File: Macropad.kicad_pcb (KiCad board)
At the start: 2 copper layers, 11 parts, among them SW1 SW_Push, SW2 SW_Push, SW3 SW_Push, SW4 SW_Push, SW5 SW_Push, U1 XIAO-RP2040-DIP

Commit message: added the libraries!!!
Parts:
- removed OL1: OLED, display:SSD1306_OLED-0.91-128x32
- added D5: SK6812MINI, LED_SMD:LED_SK6812MINI_PLCC4_3.5x3.5mm_P1.75mm, F.Cu at (191.8, 109.0)
- added J1: Conn_01x04, display:SSD1306-0.91-OLED-4pin-128x32, F.Cu at (165.8, 73.9)
- moved D1 101.6 mm to (115.5, 79.9)
- moved D3 59.5 mm to (114.5, 108.7)
- moved D2 58.4 mm to (92.1, 108.7), turned to 180 degrees
- moved SW2 56.9 mm to (111.1, 127.8), turned to 180 degrees
- moved SW1 56.3 mm to (90.0, 127.8), turned to 180 degrees
- moved SW5 48.5 mm to (94.8, 74.8)
- moved U1 37.7 mm to (142.7, 80.1)
- moved D4 25.8 mm to (171.4, 109.0)
- moved SW3 22.8 mm to (168.3, 127.8), turned to 180 degrees
- moved SW4 22.8 mm to (189.7, 127.8), turned to 180 degrees
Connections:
- D4 pad 1: unconnected-(D4-DOUT-Pad1) -> Net-(D4-DOUT)
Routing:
- net GND: track 0.00 -> 330.3 mm
- net +5V: track 0.00 -> 276.2 mm
- net Net-(U1-GPIO3/MOSI): track 0.00 -> 80.1 mm
- net Net-(J1-Pin_4): track 0.00 -> 76.1 mm
- net Net-(J1-Pin_3): track 0.00 -> 69.7 mm
- net Net-(U1-GPIO1/RX): track 0.00 -> 62.5 mm
- net Net-(U1-GPIO4/MISO): track 0.00 -> 62.3 mm
- net Net-(D3-DOUT): track 0.00 -> 62.2 mm
- net Net-(U1-GPIO0/TX): track 0.00 -> 51.0 mm
- net Net-(U1-GPIO2/SCK): track 0.00 -> 51.0 mm
- net Net-(D1-DOUT): track 0.00 -> 38.5 mm
- net Net-(D4-DOUT): track 0.00 -> 25.5 mm
- net Net-(D2-DOUT): track 0.00 -> 23.0 mm
- net Net-(D1-DIN): track 0.00 -> 19.1 mm
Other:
- board outline added: 132.6 x 63.9 mm
- board text added: "/ / , -‐─‐- ..__／'￣｀ ＿ , -‐ｧ′/／／ ￣￣｀ //⌒＝ミ, | | | ／ ./ / ／ ⌒＼＼| | | / .::| ｛// ／ ＼ｉ | | . / .: .:| 〃 ／ ／／ j | | | ′ .: .::｣_// ／ ,_／／〃 / i∨ハ i : .:| Y{ 〃__彡'＾く／/ //ii i ! |( ∨ / ! .::|||l.|｢ //ｨﾃそk 彡 / ／_⌒| ! j :| ｀. ∨ / . i |__/|: //|弋ｚｿ ／イｯ'てトJ / /} ハ : ∨ / . | :.:.V|/V｜ ヒ ｿ ﾉj/ /ｨ/ '. ∨ / . | :.:.:!i|l「ﾍ.ﾄ, ､ ' __ 〃 〃/{ :. : i∨ . | :.:.:.:|!ﾏ={{ ＼ ＿ｰ‐ |ｉｉ| .ｲ / /イ{｛ :. :. i'. / . | :.:.:.Vﾊ ＼/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"
- board text added: ":p"
- board text added: "CO0l macropad"
- board text added: "SHOUTOUT TO MY BESTIES TACO AND 1-15 :3"
- board text added: "XIAO HERE!"
- board text added: "thx to blueprint by hackclub and amd"
- board text added: "初音ミク"

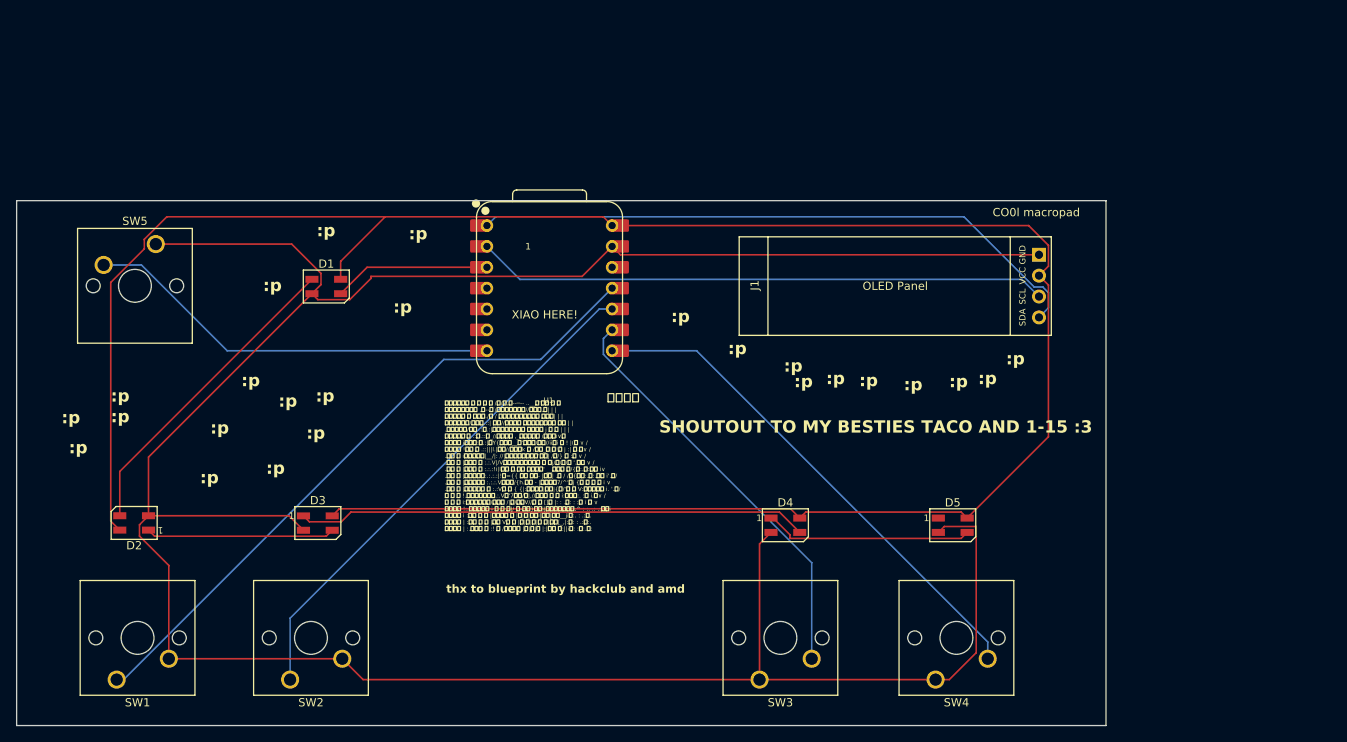
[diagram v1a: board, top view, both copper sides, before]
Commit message: the design was too big so I compacted it
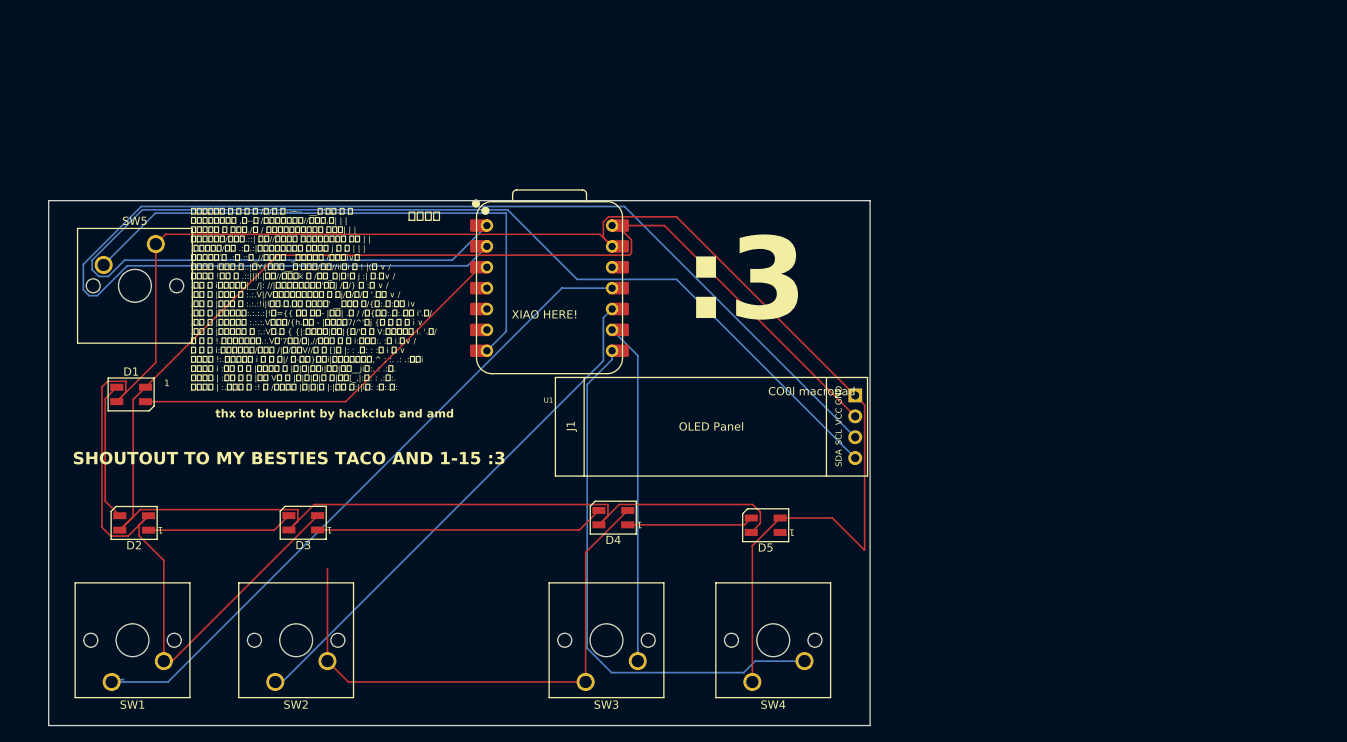
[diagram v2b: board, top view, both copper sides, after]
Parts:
- moved J1 28.2 mm to (143.4, 91.0)
- moved D1 27.2 mm to (91.8, 93.1)
- moved D5 22.8 mm to (169.0, 109.0), turned to 180 degrees
- moved SW4 22.3 mm to (167.4, 128.1)
- moved SW3 21.2 mm to (147.1, 128.1)
- moved D4 21.0 mm to (150.4, 108.1), turned to 180 degrees
- moved SW2 1.83 mm to (109.3, 128.1)
- moved D3 1.78 mm to (112.7, 108.7), turned to 180 degrees
- moved SW1 0.67 mm to (89.4, 128.1)
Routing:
- net Net-(J1-Pin_3): track 69.7 -> 163.5 mm
- net Net-(J1-Pin_4): track 76.1 -> 160.1 mm
- net +5V: track 276.2 -> 221.2 mm
- net Net-(D1-DIN): track 19.1 -> 47.5 mm
- net Net-(D3-DOUT): track 62.2 -> 35.2 mm
- net Net-(D1-DOUT): track 38.5 -> 17.0 mm
- net Net-(U1-GPIO0/TX): track 51.0 -> 69.4 mm
- net GND: track 330.3 -> 316.7 mm
- net Net-(D4-DOUT): track 25.5 -> 15.4 mm
- net Net-(U1-GPIO2/SCK): track 51.0 -> 41.6 mm
- net Net-(D2-DOUT): track 23.0 -> 17.8 mm
- net Net-(U1-GPIO1/RX): track 62.5 -> 65.7 mm
- net Net-(U1-GPIO3/MOSI): track 80.1 -> 81.6 mm
- net Net-(U1-GPIO4/MISO): track 62.3 -> 62.9 mm
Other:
- board size 132.6 x 63.9 mm -> 100 x 63.9 mm
- board text added: ":3"
- board text removed: ":p"
